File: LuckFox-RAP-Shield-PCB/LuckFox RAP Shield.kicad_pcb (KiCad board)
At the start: 2 copper layers, 21.3 x 28.4 mm, 4 parts, among them J1 LuckFox_Pico_Mini_Connector, J2 External_5V_Input_from_Buck_M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, U2 W5500_Ethernet_Module_DNP_on_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

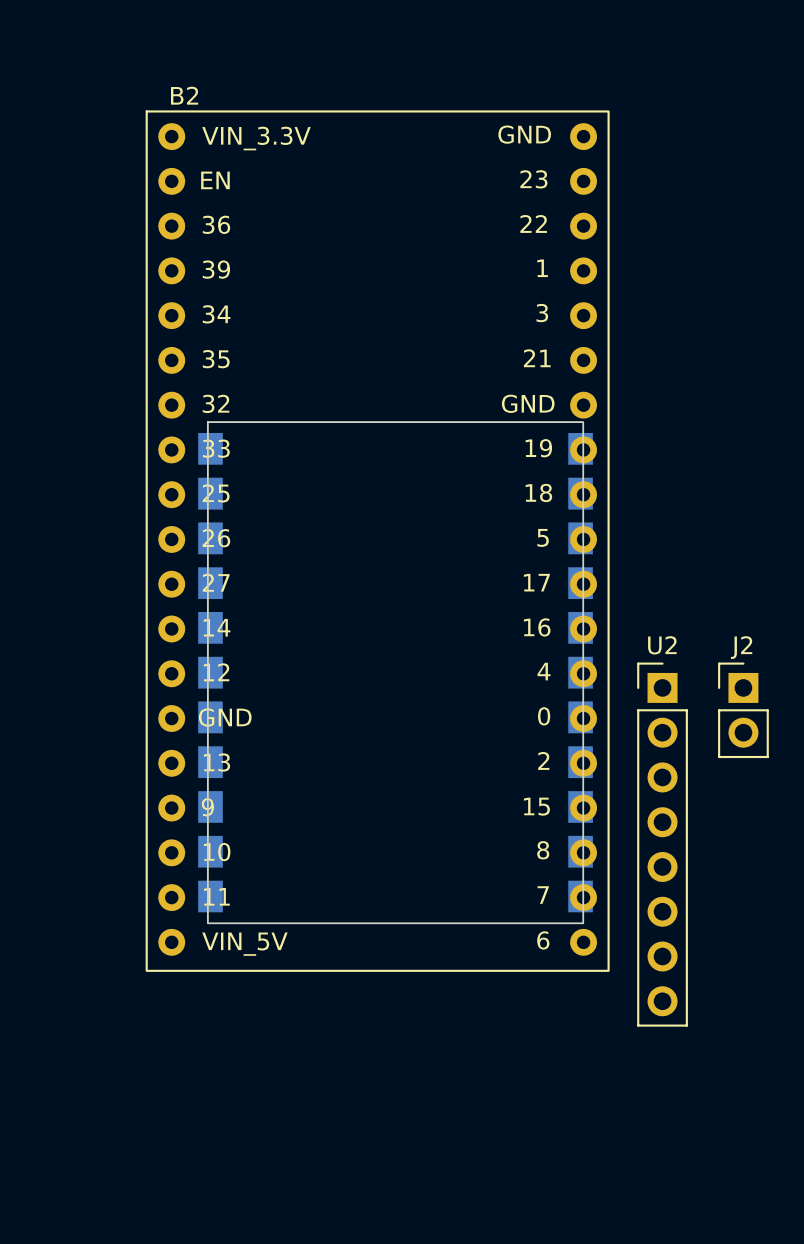
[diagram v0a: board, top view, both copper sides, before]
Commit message: Re-center J1 for the corrected (margin-free) ESP32 board length
B2's board center moved from local (13.97, 31.695) to (13.97, 26.67)
now that the footprint's true length is 53.34mm, not 63.39mm. Also
picked up B2's and J1's latest positions from your own KiCad edits
(both had moved since the last commit). J1 recentered at (124.8,
94.52) using the current B2 position (121.33, 81.92).
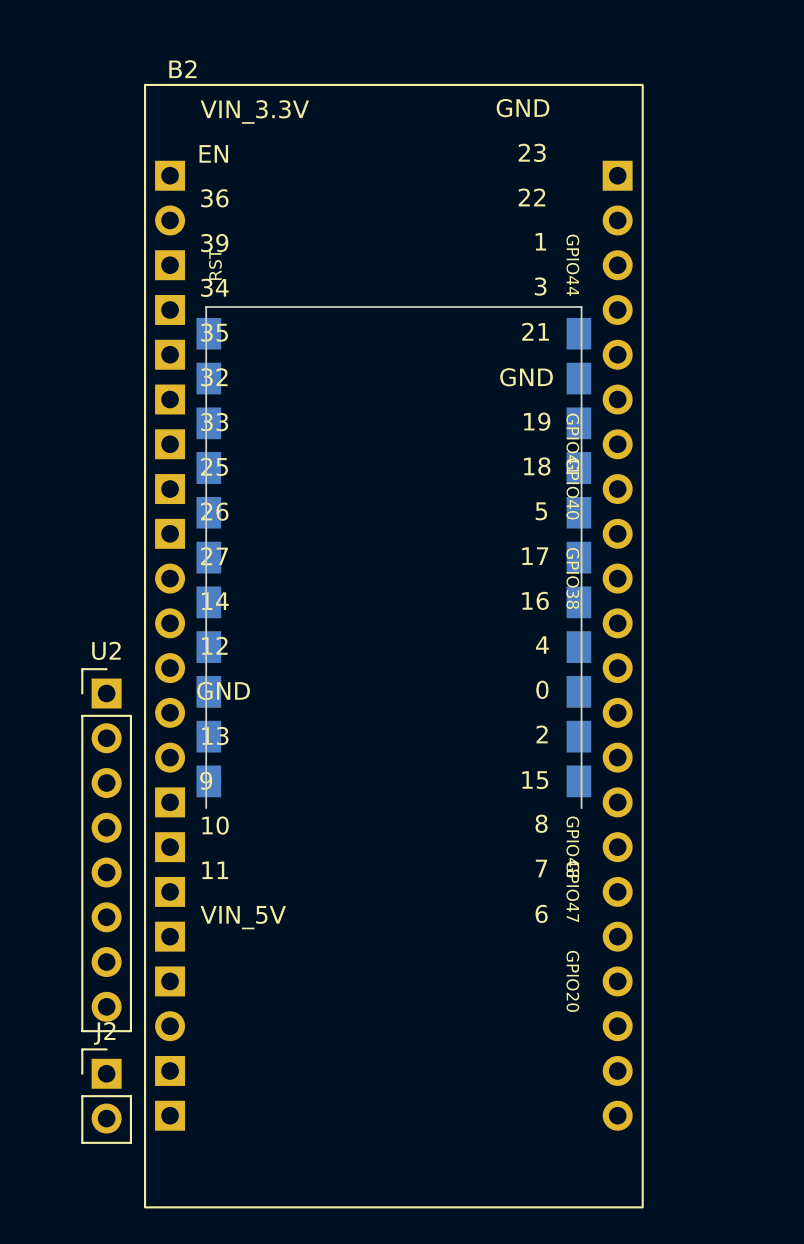
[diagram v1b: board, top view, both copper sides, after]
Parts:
- moved J2 42.3 mm to (119.0, 137.9)
- moved U2 31.5 mm to (119.0, 116.3)
- moved J1 6.53 mm to (124.8, 94.5)
- moved B2 1.51 mm to (121.3, 81.9)

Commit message: Re-center J1 for the margin-corrected ESP32 footprint
B2's board center shifted to local (13.97, 27.52) with the added
0.85mm edge margin. J1 recentered at (124.8, 95.37) using B2's current
position (121.33, 81.92); also picked up that J1 had moved again in
your own session since the last commit.
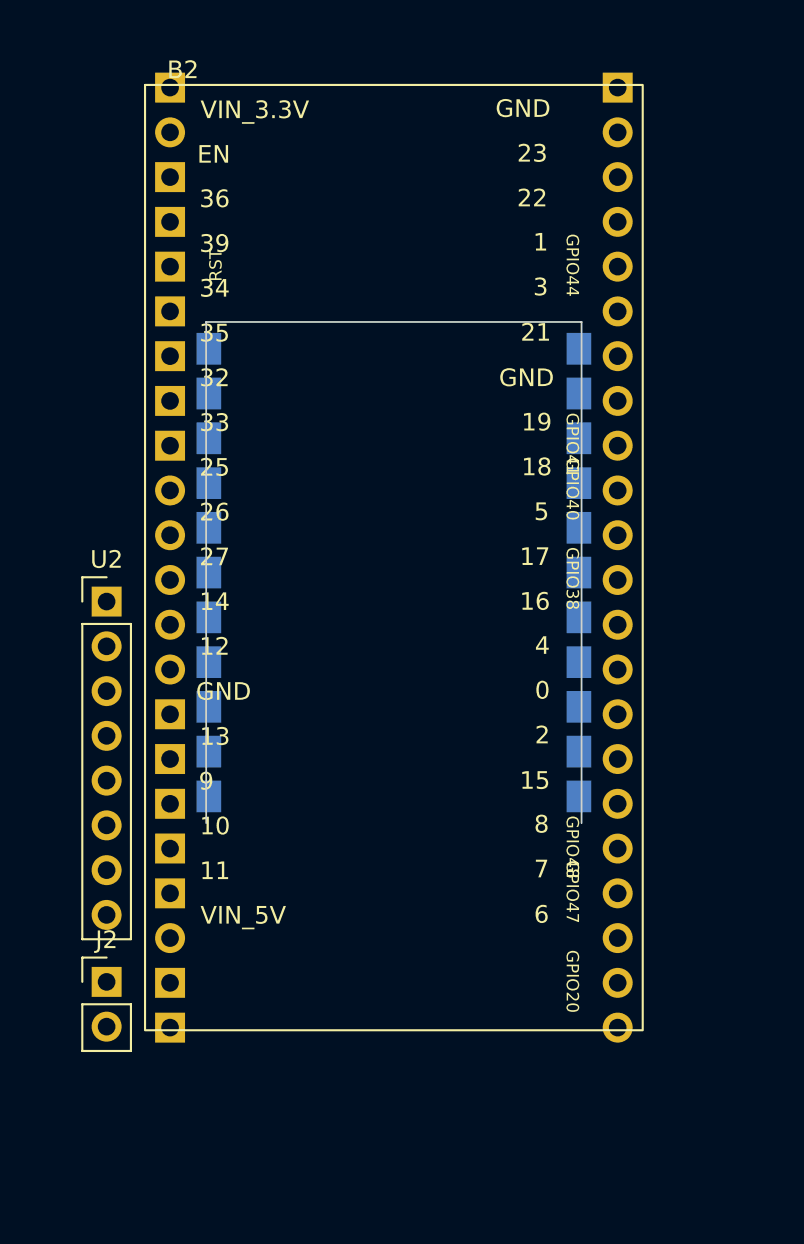
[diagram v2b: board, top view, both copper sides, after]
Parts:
- moved J2 5.22 mm to (119.0, 132.7)
- moved U2 5.22 mm to (119.0, 111.1)
- moved J1 0.85 mm to (124.8, 95.4)
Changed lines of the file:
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@@
 		(layer "F.Cu")
 		(at 121.33 81.92)
-		(descr "Real ESP32-S3-WROOM-1 DevKitC-1 dual-USB-C variant, 44 pins (22/row), 2.54mm pitch, 25.40mm row spacing (1.27mm inset from each edge on a 27.94mm-wide board). Pin labels and this shield's schematic-pin-number mapping are per the board's own silkscreen GPIO numbers -- confirmed against a full pinout diagram. Vertical pin-field placement (5mm top margin) is an estimate from partial dimensions, not a direct measurement; verify against the real board if silkscreen alignment matters.")
+		(descr "Real ESP32-S3-WROOM-1 DevKitC-1 dual-USB-C variant, 44 pins (22/row), 2.54mm pitch, 25.40mm row spacing (1.27mm inset from each edge on a 27.94mm-wide board). Pin labels and this shield's schematic-pin-number mapping are per the board's own silkscreen GPIO numbers -- confirmed against a full pinout diagram. Board length equals the pin-to-pin span exactly (53.34mm, 21 gaps x 2.54mm), zero top/bottom margin, per direct user measurement -- first pin row is flush with the top edge, last pin row flush with the bottom edge.")
 		(property "Reference" "B2"
 			(at 2 -1 0)
@@
 		(fp_rect
 			(start -0.15 -0.15)
-			(end 28.09 63.54)
+			(end 28.09 53.49)
 			(stroke
 				(width 0.12)
@@
 		(fp_rect
 			(start -0.4 -0.4)
-			(end 28.34 63.79)
+			(end 28.34 53.74)
 			(stroke
 				(width 0.05)
@@
 		(fp_rect
 			(start 0 0)
-			(end 27.94 63.39)
+			(end 27.94 53.34)
 			(stroke
 				(width 0.1)
@@
 		)
 		(pad "1" thru_hole rect
-			(at 1.27 55.8 90)
+			(at 1.27 50.8 90)
 			(size 1.7 1.7)
 			(drill 1)
@@
 		)
 		(pad "2" thru_hole rect
-			(at 1.27 5 90)
+			(at 1.27 0 90)
 			(size 1.7 1.7)
 			(drill 1)
@@
 		)
 		(pad "3" thru_hole rect
-			(at 1.27 58.34 90)
+			(at 1.27 53.34 90)
 			(size 1.7 1.7)
 			(drill 1)
@@
 		)
 		(pad "3V3_B" thru_hole circle
-			(at 1.27 7.54 90)
+			(at 1.27 2.54 90)
 			(size 1.7 1.7)
 			(drill 1)
@@
 		)
 		(pad "4" thru_hole rect
-			(at 1.27 10.08 90)
+			(at 1.27 5.08 90)
 			(size 1.7 1.7)
 			(drill 1)
@@
 		)
 		(pad "5" thru_hole rect
-			(at 1.27 12.62 90)
+			(at 1.27 7.62 90)
 			(size 1.7 1.7)
 			(drill 1)
@@
 		)
 		(pad "6" thru_hole rect
-			(at 1.27 15.16 90)
+			(at 1.27 10.16 90)
 			(size 1.7 1.7)
 			(drill 1)
@@
 		)
 		(pad "7" thru_hole rect
-			(at 1.27 17.7 90)
+			(at 1.27 12.7 90)
 			(size 1.7 1.7)
 			(drill 1)
@@
 		)
 		(pad "8" thru_hole rect
-			(at 1.27 20.24 90)
+			(at 1.27 15.24 90)
 			(size 1.7 1.7)
 			(drill 1)
@@
 		)
 		(pad "9" thru_hole rect
-			(at 1.27 40.56 90)
+			(at 1.27 35.56 90)
 			(size 1.7 1.7)
 			(drill 1)
@@
 		)
 		(pad "10" thru_hole rect
-			(at 1.27 43.1 90)
+			(at 1.27 38.1 90)
 			(size 1.7 1.7)
 			(drill 1)
@@
 		)
 		(pad "11" thru_hole rect
-			(at 1.27 45.64 90)
+			(at 1.27 40.64 90)
 			(size 1.7 1.7)
 			(drill 1)
@@
 		)
 		(pad "12" thru_hole rect
-			(at 1.27 48.18 90)
+			(at 1.27 43.18 90)
 			(size 1.7 1.7)
 			(drill 1)
@@
 		)
 		(pad "13" thru_hole rect
-			(at 1.27 50.72 90)
+			(at 1.27 45.72 90)
 			(size 1.7 1.7)
 			(drill 1)
@@
 		)
 		(pad "14" thru_hole rect
-			(at 1.27 22.78 90)
+			(at 1.27 17.78 90)
 			(size 1.7 1.7)
 			(drill 1)
@@
 		)
 		(pad "15" thru_hole rect
-			(at 1.27 25.32 90)
+			(at 1.27 20.32 90)
 			(size 1.7 1.7)
 			(drill 1)
@@
 		)
 		(pad "16" thru_hole rect
-			(at 26.67 5 270)
+			(at 26.67 0 270)
 			(size 1.7 1.7)
 			(drill 1)
@@
 		)
 		(pad "GND_C" thru_hole circle
-			(at 26.67 55.8 270)
+			(at 26.67 50.8 270)
 			(size 1.7 1.7)
 			(drill 1)
@@
 		)
 		(pad "GND_D" thru_hole circle
-			(at 26.67 58.34 270)
+			(at 26.67 53.34 270)
 			(size 1.7 1.7)
 			(drill 1)
@@
 		)
 		(pad "GPIO0" thru_hole circle
-			(at 26.67 38.02 270)
+			(at 26.67 33.02 270)
 			(size 1.7 1.7)
 			(drill 1)
@@
 		)
 		(pad "GPIO1" thru_hole circle
-			(at 26.67 12.62 270)
+			(at 26.67 7.62 270)
 			(size 1.7 1.7)
 			(drill 1)
@@
 		)
 		(pad "GPIO2" thru_hole circle
-			(at 26.67 15.16 270)
+			(at 26.67 10.16 270)
 			(size 1.7 1.7)
 			(drill 1)
@@
 		)
 		(pad "GPIO3" thru_hole circle
-			(at 1.27 35.48 90)
+			(at 1.27 30.48 90)
 			(size 1.7 1.7)
 			(drill 1)
@@
 		)
 		(pad "GPIO8" thru_hole circle
-			(at 1.27 32.94 90)
+			(at 1.27 27.94 90)
 			(size 1.7 1.7)
 			(drill 1)
@@
 		)
 		(pad "GPIO14" thru_hole circle
-			(at 1.27 53.26 90)
+			(at 1.27 48.26 90)
 			(size 1.7 1.7)
 			(drill 1)
@@
 		)
 		(pad "GPIO17" thru_hole circle
-			(at 1.27 27.86 90)
+			(at 1.27 22.86 90)
 			(size 1.7 1.7)
 			(drill 1)
@@
 		)
 		(pad "GPIO18" thru_hole circle
-			(at 1.27 30.4 90)
+			(at 1.27 25.4 90)
 			(size 1.7 1.7)
 			(drill 1)
@@
 		)
 		(pad "GPIO19" thru_hole circle
-			(at 26.67 53.26 270)
+			(at 26.67 48.26 270)
 			(size 1.7 1.7)
 			(drill 1)
@@
 		)
 		(pad "GPIO20" thru_hole circle
-			(at 26.67 50.72 270)
+			(at 26.67 45.72 270)
 			(size 1.7 1.7)
 			(drill 1)
@@
 		)
 		(pad "GPIO21" thru_hole circle
-			(at 26.67 48.18 270)
+			(at 26.67 43.18 270)
 			(size 1.7 1.7)
 			(drill 1)
@@
 		)
 		(pad "GPIO35" thru_hole circle
-			(at 26.67 35.48 270)
+			(at 26.67 30.48 270)
 			(size 1.7 1.7)
 			(drill 1)
@@
 		)
 		(pad "GPIO36" thru_hole circle
-			(at 26.67 32.94 270)
+			(at 26.67 27.94 270)
 			(size 1.7 1.7)
 			(drill 1)
@@
 		)
 		(pad "GPIO37" thru_hole circle
-			(at 26.67 30.4 270)
+			(at 26.67 25.4 270)
 			(size 1.7 1.7)
 			(drill 1)
@@
 		)
 		(pad "GPIO38" thru_hole circle
-			(at 26.67 27.86 270)
+			(at 26.67 22.86 270)
 			(size 1.7 1.7)
 			(drill 1)
@@
 		)
 		(pad "GPIO39" thru_hole circle
-			(at 26.67 25.32 270)
+			(at 26.67 20.32 270)
 			(size 1.7 1.7)
 			(drill 1)
@@
 		)
 		(pad "GPIO40" thru_hole circle
-			(at 26.67 22.78 270)
+			(at 26.67 17.78 270)
 			(size 1.7 1.7)
 			(drill 1)
@@
 		)
 		(pad "GPIO41" thru_hole circle
-			(at 26.67 20.24 270)
+			(at 26.67 15.24 270)
 			(size 1.7 1.7)
 			(drill 1)
@@
 		)
 		(pad "GPIO42" thru_hole circle
-			(at 26.67 17.7 270)
+			(at 26.67 12.7 270)
 			(size 1.7 1.7)
 			(drill 1)
@@
 		)
 		(pad "GPIO43" thru_hole circle
-			(at 26.67 7.54 270)
+			(at 26.67 2.54 270)
 			(size 1.7 1.7)
 			(drill 1)
@@
 		)
 		(pad "GPIO44" thru_hole circle
-			(at 26.67 10.08 270)
+			(at 26.67 5.08 270)
 			(size 1.7 1.7)
 			(drill 1)
@@
 		)
 		(pad "GPIO45" thru_hole circle
-			(at 26.67 40.56 270)
+			(at 26.67 35.56 270)
 			(size 1.7 1.7)
 			(drill 1)
@@
 		)
 		(pad "GPIO46" thru_hole circle
-			(at 1.27 38.02 90)
+			(at 1.27 33.02 90)
 			(size 1.7 1.7)
 			(drill 1)
@@
 		)
 		(pad "GPIO47" thru_hole circle
-			(at 26.67 45.64 270)
+			(at 26.67 40.64 270)
 			(size 1.7 1.7)
 			(drill 1)
@@
 		)
 		(pad "GPIO48" thru_hole circle
-			(at 26.67 43.1 270)
+			(at 26.67 38.1 270)
 			(size 1.7 1.7)
 			(drill 1)
@@
 	(footprint "Connector_PinHeader_2.54mm:PinHeader_1x08_P2.54mm_Vertical"
 		(layer "F.Cu")
-		(at 119 116.3)
+		(at 119 111.085)
 		(descr "Through hole straight pin header, 1x08, 2.54mm pitch, single row")
 		(tags "Through hole pin header THT 1x08 2.54mm single row")
@@
 	(footprint "Connector_PinHeader_2.54mm:PinHeader_1x02_P2.54mm_Vertical"
 		(layer "F.Cu")
-		(at 119 137.88)
+		(at 119 132.665)
 		(descr "Through hole straight pin header, 1x02, 2.54mm pitch, single row")
 		(tags "Through hole pin header THT 1x02 2.54mm single row")
@@
 	(footprint "footprints:LuckFox_Pico_Mini"
 		(layer "B.Cu")
-		(at 124.8 94.52)
+		(at 124.8 95.37)
 		(descr "Cutout + edge-castellation mount for LuckFox Pico Mini, MIRRORED (component side, incl. camera FPC connector, faces AWAY from the shield -- accessible from outside once assembled) -- module nests underneath the shield through this slot. U-shaped opening: enclosed on left/right/top, OPEN on the bottom edge (the USB-C end, post-mirror) so the module's USB-C connector can extend past the shield's own board edge. The open side only works if this footprint is positioned so that opening actually reaches your board's real outer edge -- it is not automatically merged with your board outline. 22 castellated edge pads lap-solder directly to the pads here -- no header/socket. Cutout sized to LuckFox's 21.00x28.14mm outline plus 0.15mm clearance per side; pads centered on LuckFox's nominal edge line (2.54mm pitch, 17.78mm row spacing, per LuckFox's official mechanical drawing) so they straddle the routed slot edge. Pin-row order is reversed vs the unmirrored version: real pin 11/12 (camera-connector end) are now at the top (y=1.37), real pin 1/22 (USB-C end) now at the bottom (y=26.77). Confirm the 0.15mm clearance and pad size against your fab house's minimum slot/annular tolerances before ordering.")
 		(property "Reference" "J1"
@@
 		)
 		(fp_text user "12"
-			(at -6.345 18.285 0)
+			(at -6.345 13.07 0)
 			(unlocked yes)
 			(layer "B.SilkS")
